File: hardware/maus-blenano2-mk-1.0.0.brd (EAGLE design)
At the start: 18 x 21 mm, 14 parts, among them Q1 SI2301CDS, U1 REDBEAR_BLE_NANO2_LESS, U2 MCP73831T-2ACI/OT

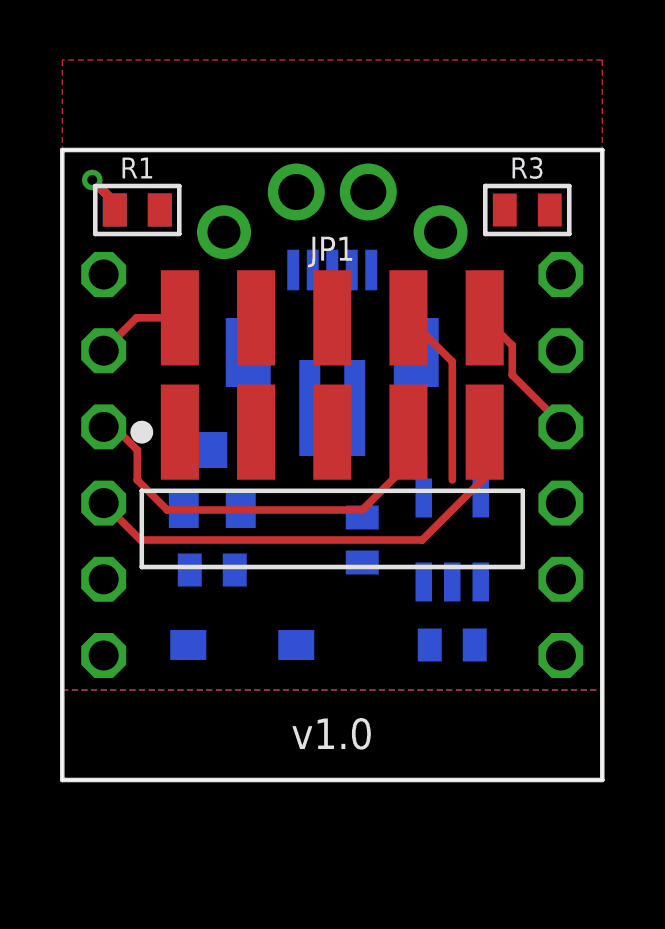
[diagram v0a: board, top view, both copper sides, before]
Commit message: initial rev of ble nano2 daughter board
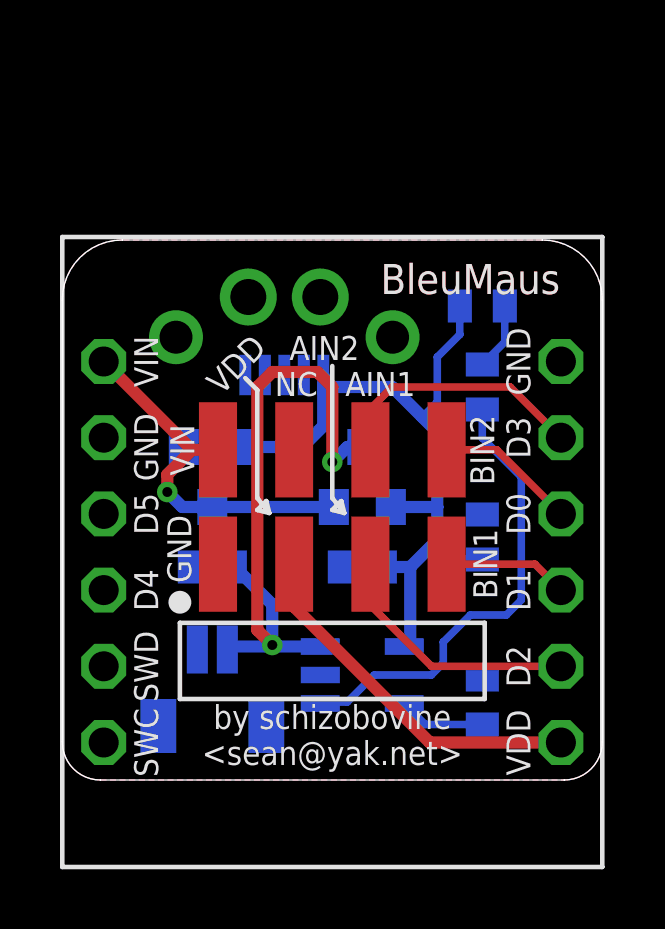
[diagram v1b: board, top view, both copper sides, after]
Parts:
- removed CHG: LED0603-TIGHT, a_parts:LED-0603-TIGHT
- removed JP1: M05X2SMD_RA, a_parts:2X5_SMD_RA
- added CHARGE: LED0603-TIGHT, a_parts:LED-0603-TIGHT
- added J1: M04X2SMD_RA, a_parts:2X4_SMD_RA
- D1: value (none) -> PMEG2005CT; device a_parts:SOD123-SCHOTTKY -> a_parts:SOT23
- JP2: value M02JST-ZH-SM4-VERT-R+ -> M02JST-SH-VERT; device a_parts:JST-2-ZH-VERT-SMD+R+ -> a_parts:JST-2-SH-VERT
- R2: value 10K -> 100K
- moved R3 16.5 mm to (14.0, 2.60), flipped to the bottom, turned to 90 degrees
- moved R1 12.9 mm to (14.0, 13.1), flipped to the bottom, turned to 270 degrees
- moved R2 9.07 mm to (14.0, 8.10), turned to 90 degrees
- moved JP2 8.85 mm to (5.00, 5.10), turned to 180 degrees
- moved C2 8.41 mm to (5.00, 7.10), turned to 0 degrees
- moved D1 5.69 mm to (5.00, 10.1), turned to 180 degrees
- moved U2 5.41 mm to (10.0, 3.50), turned to 180 degrees
- moved Q1 5.00 mm to (10.0, 10.1)
- moved USB1 3.85 mm to (7.40, 16.1)
- moved U1 2.90 mm to (9.00, 7.60)
- moved C1 0.90 mm to (10.0, 7.10), turned to 0 degrees
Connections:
- removed net IRRECV: JP1.2, U1.13
- net 3.3V: now also J1.3; no longer JP1.5
- net 5V: now also CHARGE.A, D1.2; no longer CHG.A, D1.A
- net AIN1: now also J1.6, U1.13; no longer JP1.7, U1.14
- net AIN2: now also J1.5, U1.16; no longer JP1.9, U1.15
- net BIN1: now also J1.7, U1.15; no longer JP1.8, U1.3
- net BIN2: now also J1.8, U1.14; no longer JP1.10, U1.4
- net GND: now also J1.1; no longer JP1.3
- net N$2: now also CHARGE.C; no longer CHG.C
- net VIN: now also D1.3, J1.2; no longer D1.C, JP1.1
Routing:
- net 5V: track 0.00 -> 25.9 mm
- net VBAT: track 0.00 -> 21.8 mm, vias 0 -> 2
- net N$1: track 0.00 -> 15.4 mm
- net VIN: track 0.00 -> 12.5 mm, vias 0 -> 1
- net 3.3V: track 0.00 -> 12.2 mm
- net AIN2: track 15.6 -> 8.56 mm
- net AIN1: track 13.6 -> 8.72 mm
- net IRRECV: track 2.99 -> 0.00 mm
- net N$11: track 0.00 -> 2.89 mm
- net BIN1: track 6.01 -> 4.17 mm
- net N$2: track 2.62 -> 2.26 mm, vias 1 -> 0
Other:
- board size 18 x 21 mm -> 18 x 18 mm
- board text added: "AIN1"
- board text added: "AIN2"
- board text added: "BIN1"
- board text added: "BIN2"
- board text added: "BleuMaus"
- board text added: "GND"
- board text added: "NC"
- board text added: "USB PWR ONLY"
- board text added: "VDD"
- board text added: "VIN"
- board text added: "by schizobovine <sean@yak.net>"
